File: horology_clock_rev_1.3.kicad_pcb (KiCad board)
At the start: 2 copper layers, 100 x 100 mm, 46 parts, among them J1 Conn_01x36, J10 Conn_01x08, J11 Screw_Terminal_01x02, J12 Conn_01x02, J13 Conn_01x04, J14 Conn_01x10, J2 Conn_01x36, J3 Screw_Terminal_01x02, J4 Screw_Terminal_01x02, J5 Screw_Terminal_01x02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

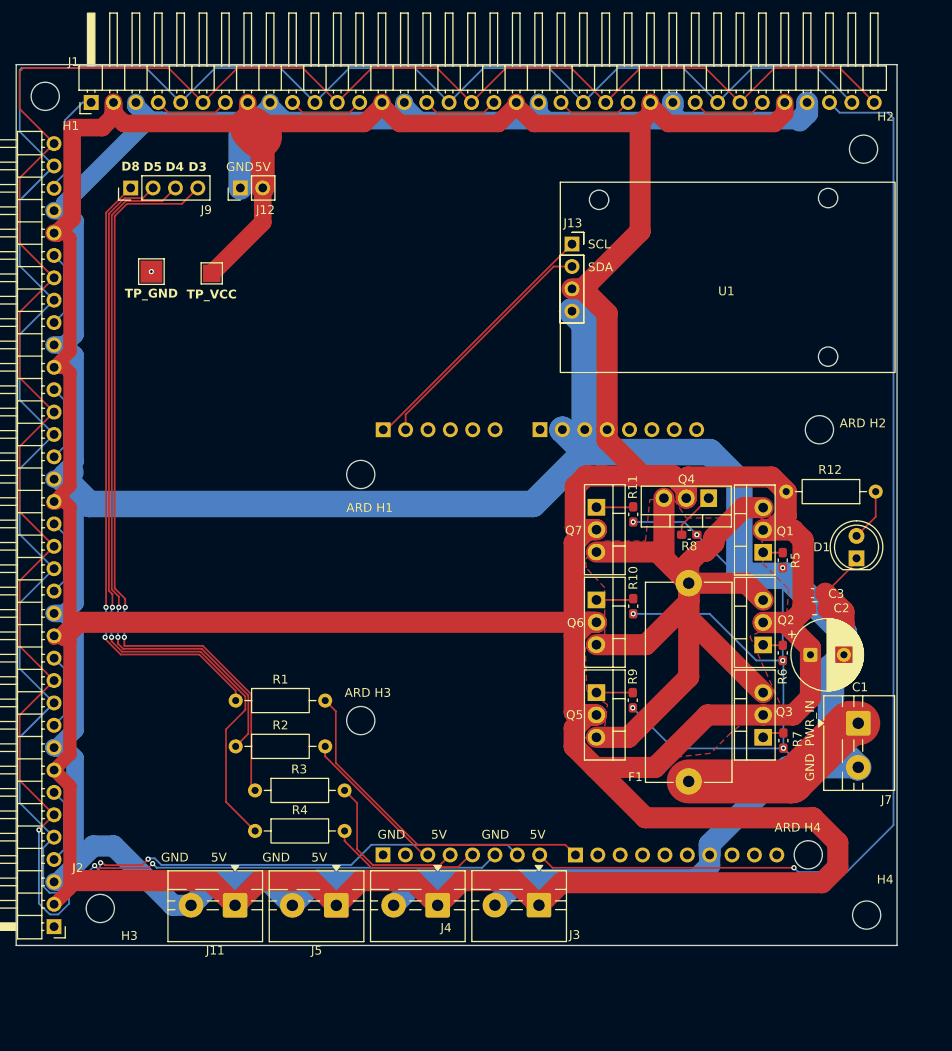
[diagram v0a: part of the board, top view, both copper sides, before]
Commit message: Grouped Data and Power ouputs into close physical units.
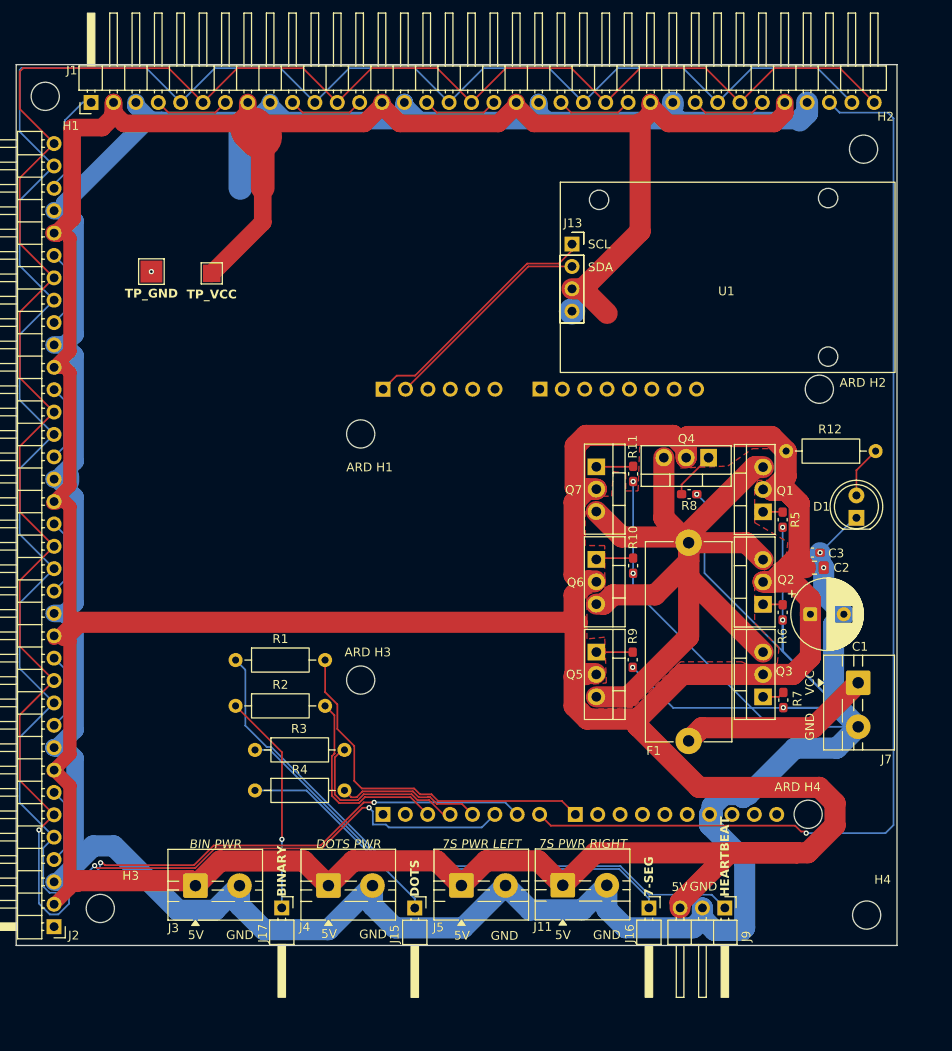
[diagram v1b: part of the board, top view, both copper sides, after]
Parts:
- removed J12: Conn_01x02, Connector_PinHeader_2.54mm:PinHeader_1x02_P2.54mm_Vertical
- added J15: Conn_01x01, Connector_PinHeader_2.54mm:PinHeader_1x01_P2.54mm_Horizontal, F.Cu at (126.2, 144.9)
- added J16: Conn_01x01, Connector_PinHeader_2.54mm:PinHeader_1x01_P2.54mm_Horizontal, F.Cu at (152.8, 144.9)
- added J17: Conn_01x01, Connector_PinHeader_2.54mm:PinHeader_1x01_P2.54mm_Horizontal, F.Cu at (111.1, 144.9)
- J9: value Conn_01x04 -> Conn_01x03; footprint Connector_PinHeader_2.54mm:PinHeader_1x04_P2.54mm_Vertical -> Connector_PinHeader_2.54mm:PinHeader_1x03_P2.54mm_Horizontal
- moved J9 106.0 mm to (161.4, 144.9), turned to -90 degrees
- moved J3 39.1 mm to (101.3, 142.4), turned to 0 degrees
- moved J11 37.3 mm to (143.0, 142.4), turned to 0 degrees
- moved J5 14.4 mm to (131.5, 142.4), turned to 0 degrees
- moved J4 12.6 mm to (116.4, 142.4), turned to 0 degrees
- moved J14 4.60 mm to (144.4, 134.3)
- moved A1 4.60 mm to (158.2, 86.0)
- moved C1 4.60 mm to (171.1, 111.6)
- moved C2 4.60 mm to (171.6, 106.3)
- moved J6 4.60 mm to (122.6, 86.0)
- moved Q1 4.60 mm to (165.7, 100.0)
- moved Q2 4.60 mm to (165.7, 110.5)
- moved Q3 4.60 mm to (165.7, 121.0)
- moved Q5 4.60 mm to (146.8, 115.9)
- moved Q6 4.60 mm to (146.8, 105.4)
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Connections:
- J9 pad 2: DOTS_DATA -> GND
- J9 pad 3: BINARY_DATA -> +5V
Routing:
- net GND: track 619.0 -> 514.9 mm, vias 8 -> 10
- net DOTS_DATA: track 90.3 -> 24.3 mm, vias 2 -> 0
- net BINARY_DATA: track 81.3 -> 25.1 mm, vias 2 -> 1
- net 7SEG_DATA: track 87.9 -> 52.8 mm, vias 2 -> 0
- net +5V: track 600.2 -> 585.8 mm
- net Net-(J10-Pin_3): track 17.4 -> 23.1 mm
- net MAX_CS: track 277.2 -> 281.5 mm
- net RTC_SDA: track 27.6 -> 24.7 mm
- net Net-(J14-3.3V): track 39.1 -> 41.8 mm
- net MAX_DIN: track 131.4 -> 129.7 mm
- net MAX_CLK: track 288.1 -> 289.7 mm
- net RTC_SCL: track 30.2 -> 28.7 mm
- net Net-(J10-Pin_5): track 17.6 -> 16.2 mm
- net Net-(J10-Pin_4): track 19.1 -> 20.2 mm
- net VIN_PROTECTED: track 100.2 -> 99.1 mm
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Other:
- board text added: "7-SEG"
- board text added: "7S PWR LEFT"
- board text added: "7S PWR RIGHT"
- board text added: "BIN PWR"
- board text added: "BINARY"
- board text added: "DOTS"
- board text added: "DOTS PWR"
- board text added: "HEARTBEAT"
- board text added: "VCC"
- board text removed: "D3"
- board text removed: "D4"
- board text removed: "D5"
- board text removed: "D8"
- board text removed: "PWR_IN"

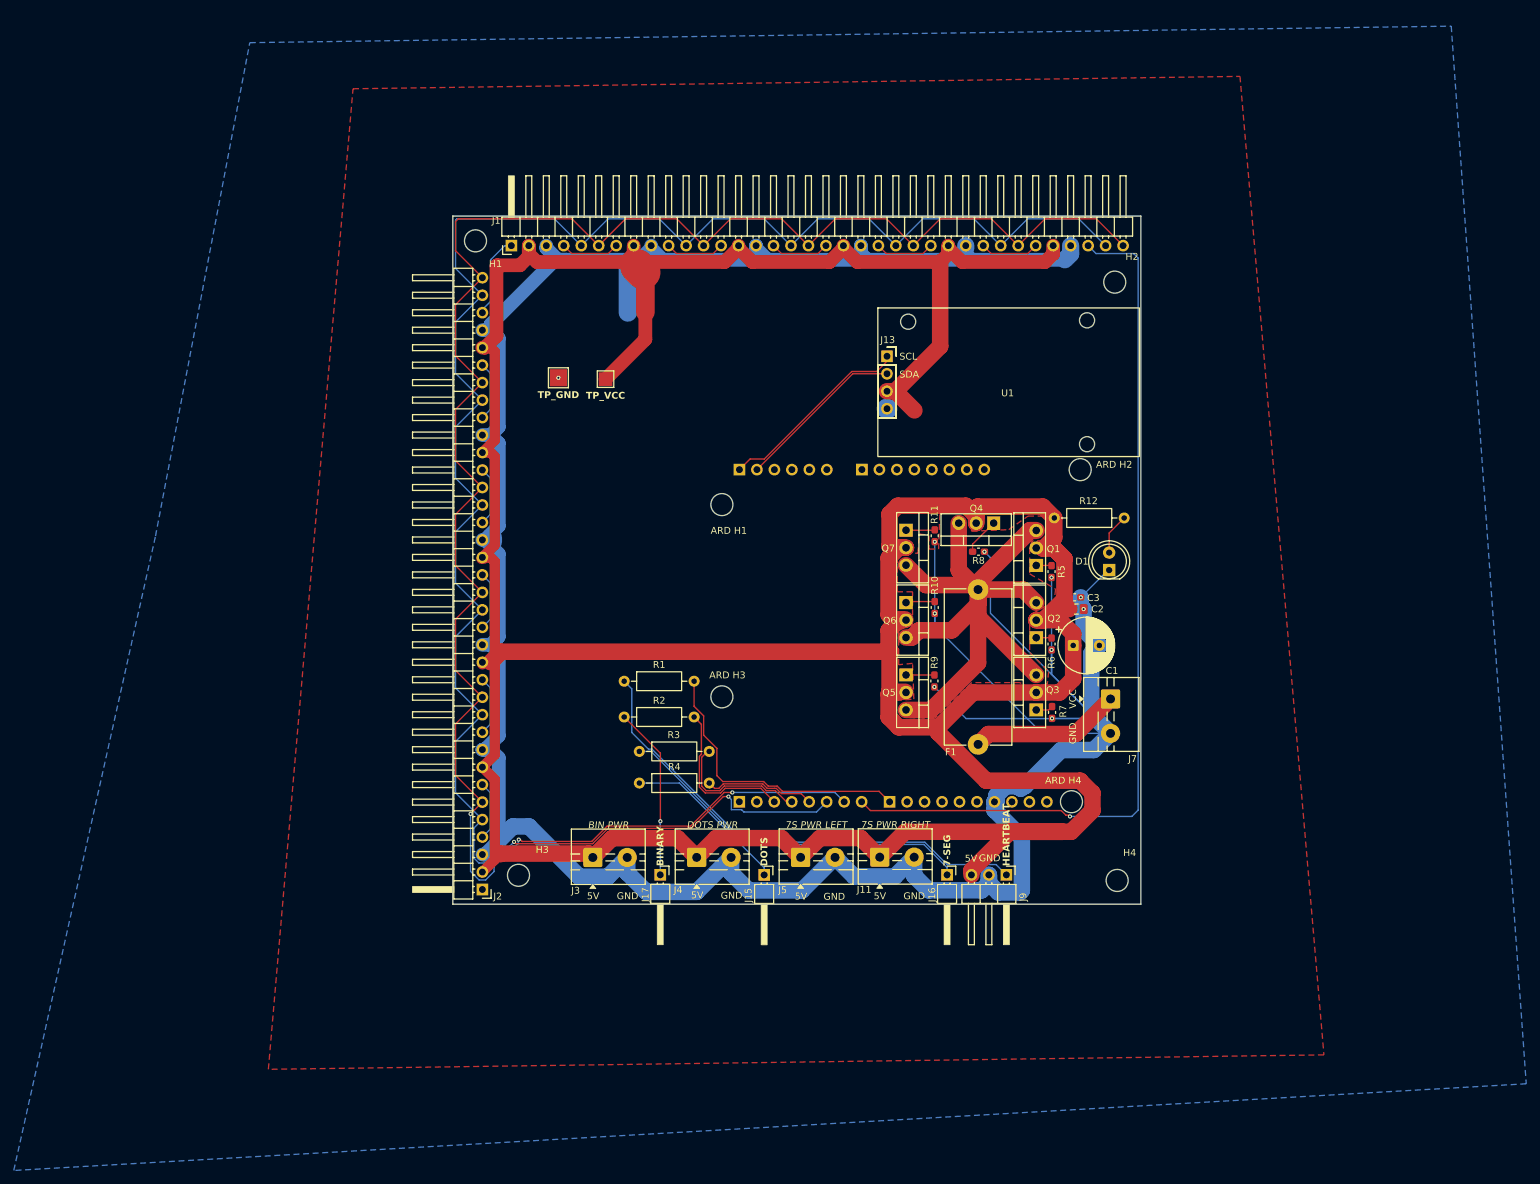
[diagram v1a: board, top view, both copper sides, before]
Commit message: Spaced the MOSFETs out around the Fuse for easy access with fat fingies.
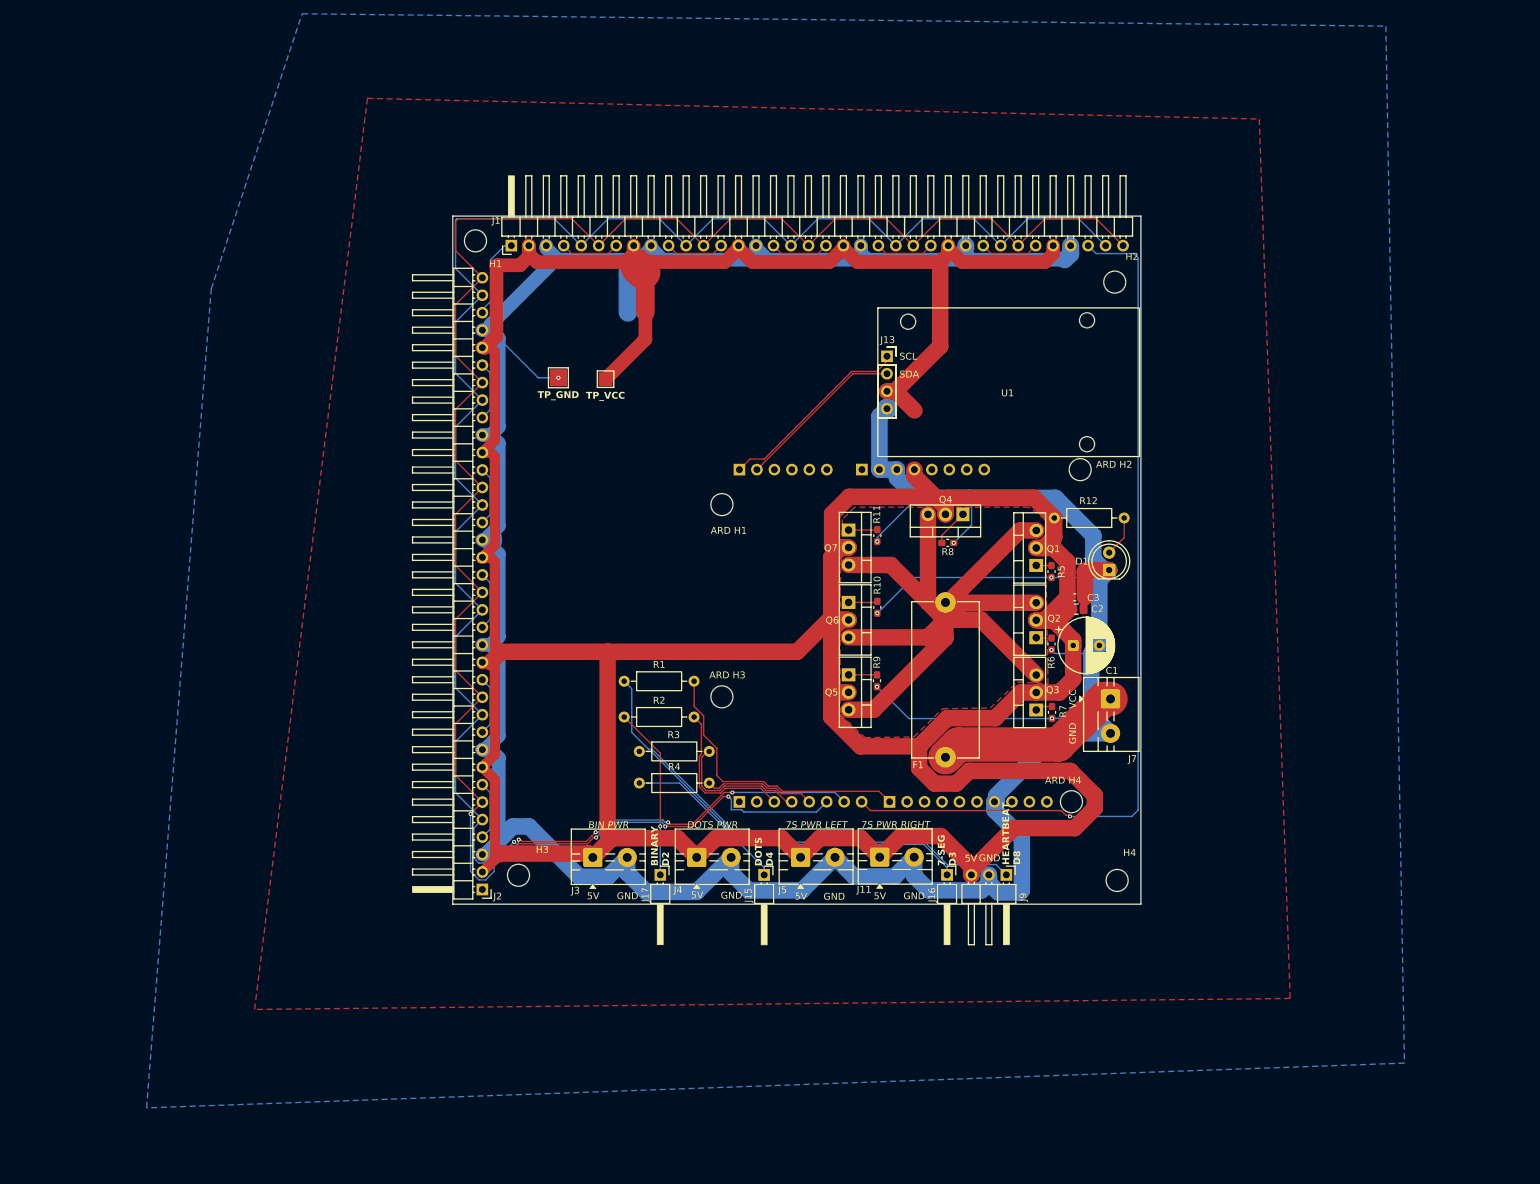
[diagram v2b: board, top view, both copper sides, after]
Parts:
- moved Q5 8.34 mm to (138.5, 115.9)
- moved Q6 8.34 mm to (138.5, 105.3)
- moved Q7 8.34 mm to (138.5, 94.8)
- moved R10 8.34 mm to (142.7, 106.1)
- moved R11 8.34 mm to (142.7, 95.6)
- moved R9 8.34 mm to (142.6, 116.7)
- moved F1 5.10 mm to (152.6, 127.8)
- moved Q4 4.64 mm to (155.1, 92.5)
- moved R8 4.64 mm to (152.9, 96.7)
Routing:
- net +5V: track 585.8 -> 630.8 mm
- net VIN_PROTECTED: track 99.1 -> 120.4 mm
- net GND: track 514.9 -> 525.8 mm, vias 10 -> 8
- net VIN_RAW: track 22.0 -> 27.5 mm
- net MAX_CLK: track 289.7 -> 290.3 mm, vias 3 -> 5
- net MAX_CS: track 281.5 -> 282.1 mm, vias 2 -> 4
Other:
- board text added: "7-SEG D3"
- board text added: "BINARY D2"
- board text added: "DOTS D4"
- board text added: "HEARTBEAT D8"
- board text removed: "7-SEG"
- board text removed: "BINARY"
- board text removed: "DOTS"
- board text removed: "HEARTBEAT"

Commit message: Moved the terminals to their final locations, and connected everything together.
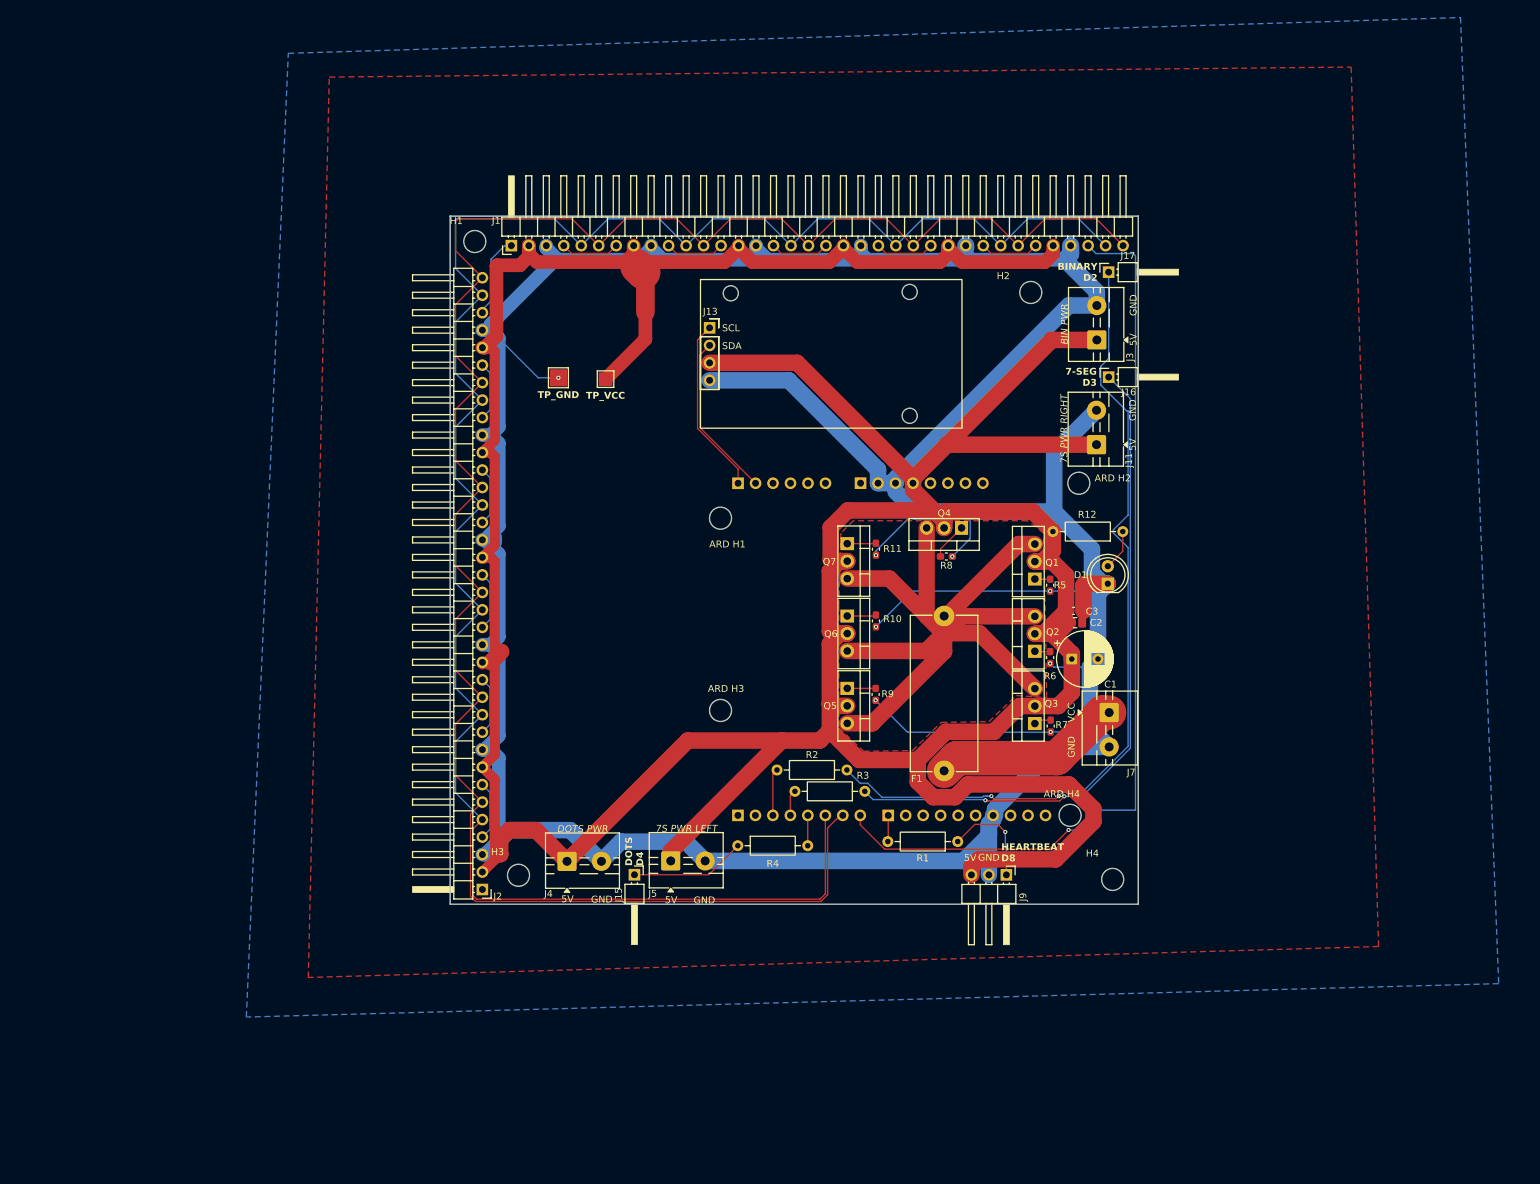
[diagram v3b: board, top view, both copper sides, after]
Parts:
- moved J17 109.2 mm to (176.3, 57.4), turned to 0 degrees
- moved J3 105.0 mm to (174.6, 67.2), turned to 90 degrees
- moved J16 76.1 mm to (176.3, 72.6), turned to 0 degrees
- moved J11 67.7 mm to (174.5, 82.4), turned to 90 degrees
- moved R1 53.8 mm to (154.3, 140.1), turned to 180 degrees
- moved R3 33.3 mm to (140.8, 132.8), turned to 180 degrees
- moved R2 33.3 mm to (138.2, 129.7), turned to 180 degrees
- moved J13 26.1 mm to (118.3, 65.5)
- moved U1 26.1 mm to (135.6, 70.8)
- moved J5 18.9 mm to (112.6, 142.9)
- moved J4 18.9 mm to (97.5, 143.0)
- moved J15 18.9 mm to (107.3, 144.9)
- moved R4 17.0 mm to (122.4, 140.7)
- moved H2 12.3 mm to (164.9, 60.3)
- moved J14 1.99 mm to (144.2, 136.3)
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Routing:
- net BINARY_DATA: track 25.1 -> 118.8 mm, vias 1 -> 2
- net HEART_BEAT_DATA: track 70.9 -> 14.7 mm, vias 0 -> 1
- net GND: track 525.8 -> 577.7 mm
- net 7SEG_DATA: track 52.8 -> 97.6 mm, vias 0 -> 2
- net Net-(J14-3.3V): track 41.8 -> 3.82 mm
- net Net-(J10-Pin_4): track 20.2 -> 3.77 mm
- net Net-(J10-Pin_3): track 23.1 -> 6.84 mm
- net Net-(J10-Pin_5): track 16.2 -> 4.41 mm
- net MAX_CS: track 282.1 -> 292.0 mm, vias 4 -> 0
- net DOTS_DATA: track 24.3 -> 16.8 mm
- net MAX_CLK: track 290.3 -> 296.8 mm, vias 5 -> 0
- net +5V: track 630.8 -> 624.6 mm
- net MAX_DIN: track 129.7 -> 133.2 mm
- net RTC_SCL: track 28.7 -> 25.7 mm
- net RTC_SDA: track 24.7 -> 24.0 mm

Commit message: Ready for Fab.
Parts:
- added G***: LOGO, LOGO, B.Cu at (95.3, 69.2)
- moved TP2 58.5 mm to (99.0, 131.2), turned to 0 degrees
- moved TP1 58.4 mm to (92.2, 131.0), turned to 0 degrees
- moved J13 6.10 mm to (124.4, 65.4)
- moved U1 6.10 mm to (141.7, 70.7)
- moved J7 5.39 mm to (174.2, 126.3), turned to 90 degrees
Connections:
- J7 pad 1: VIN_RAW -> GND
- J7 pad 2: GND -> VIN_RAW
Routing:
- net +5V: track 624.6 -> 600.0 mm
- net MAX_DIN: track 133.2 -> 124.4 mm
- net GND: track 577.7 -> 570.3 mm
- net HEART_BEAT_DATA: track 14.7 -> 11.4 mm
- net RTC_SDA: track 24.0 -> 21.5 mm
- net RTC_SCL: track 25.7 -> 23.9 mm
- net BINARY_DATA: track 118.8 -> 120.7 mm
- net VIN_RAW: track 27.5 -> 26.1 mm
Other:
- board text added: ":)"
- board text added: "Design Tomek Dobrowolski Contributors Thomas Cohu Oli Raffio-Curd Jack Byrne Charlie Baker Supervisor Mr Smith"
- board text added: "Horology Clock VCJ Enrichment 2025-2026"
- board text added: "JLCJLCJLCJLC"
- board text added: "PWR INPUT"
- board text added: "REV A - It works (probably) March 2026 Victoria College"
- board text added: "TP_5V"
- board text added: "Time well wasted."
- board text added: "https://github.com/tomekjersey0/horology_clock"
- board text removed: "CLK"
- board text removed: "CS"
- board text removed: "DIN"
- board text removed: "TP_VCC"
- board text removed: "VCC"
